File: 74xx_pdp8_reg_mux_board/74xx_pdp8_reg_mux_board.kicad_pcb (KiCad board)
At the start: 2 copper layers, 36 parts, among them P1 DIL24, P2 DIL24, P3 DIL24, P4 DIL24, P5 DIL24, P6 DIL24, U1 74LS251, U10 74LS251, U11 74LS125, U12 74LS251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

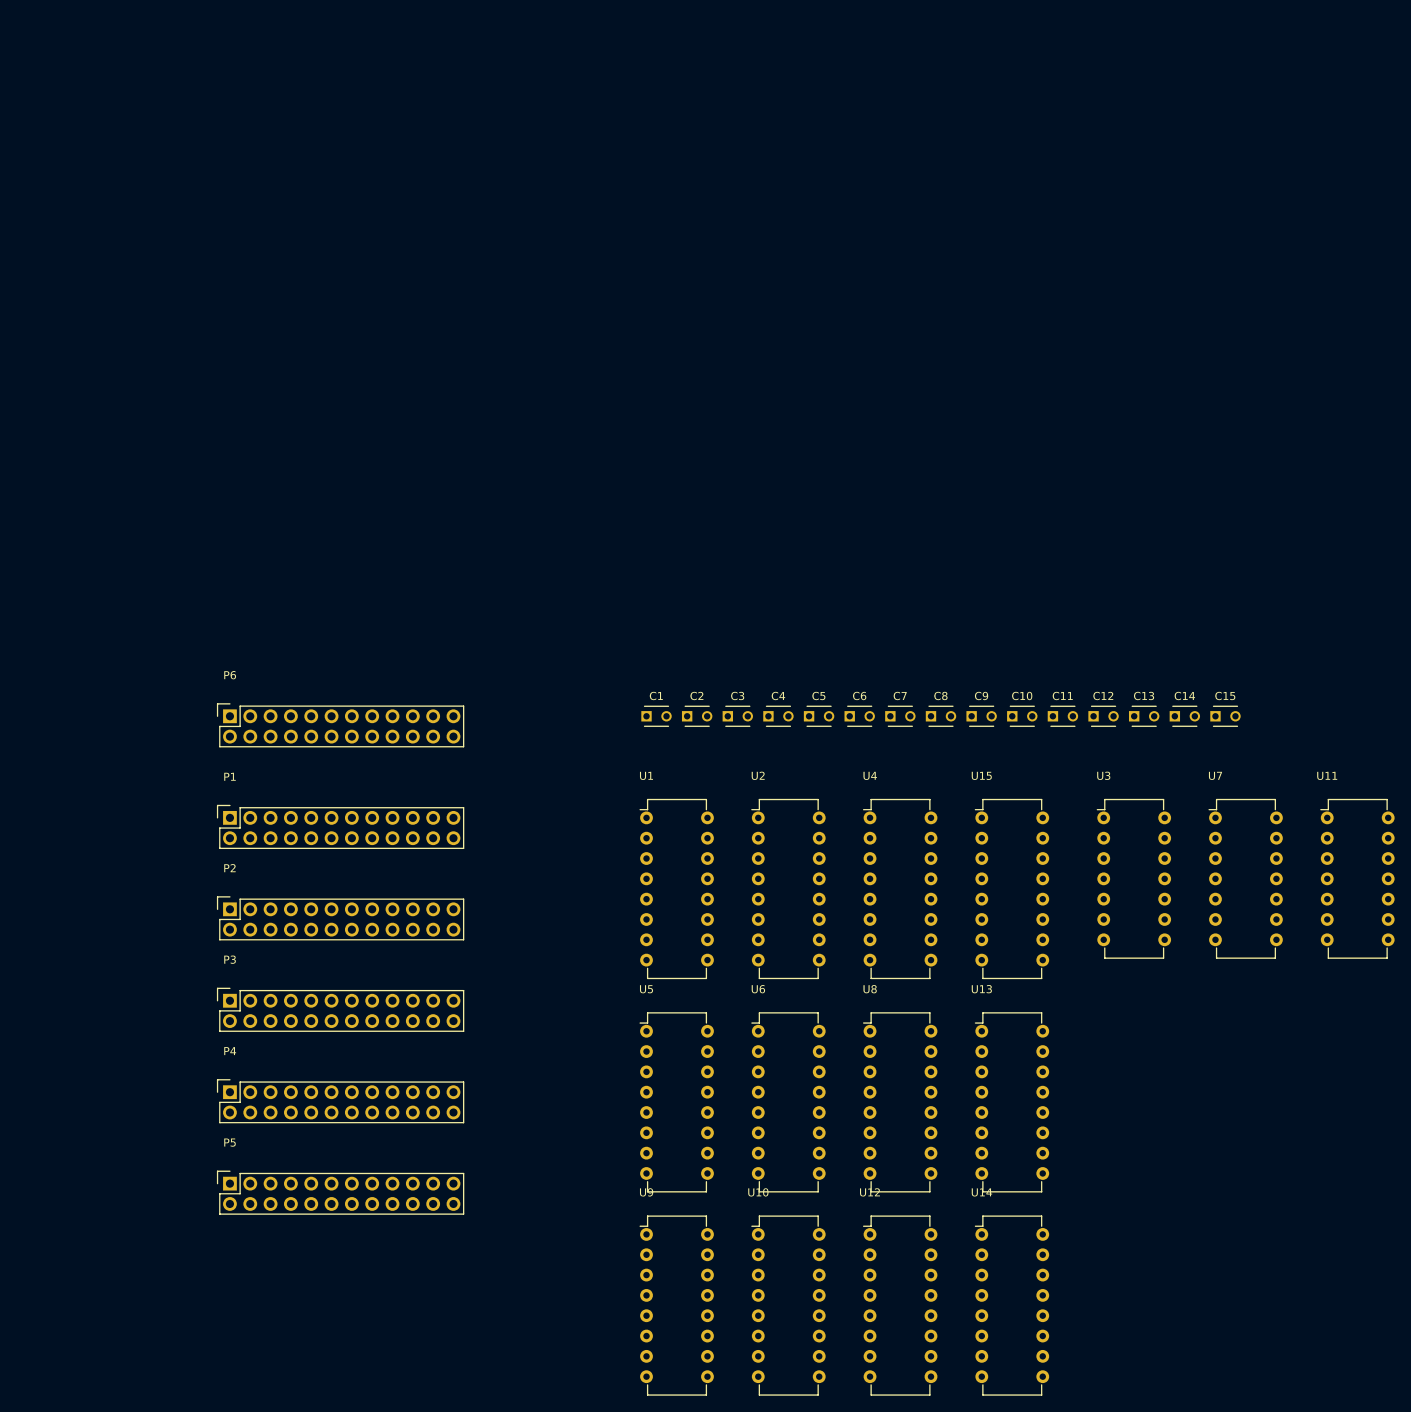
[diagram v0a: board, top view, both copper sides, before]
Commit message: Roughed-out layout of register multiplexor board. Need to double check dimensions of twin register board.
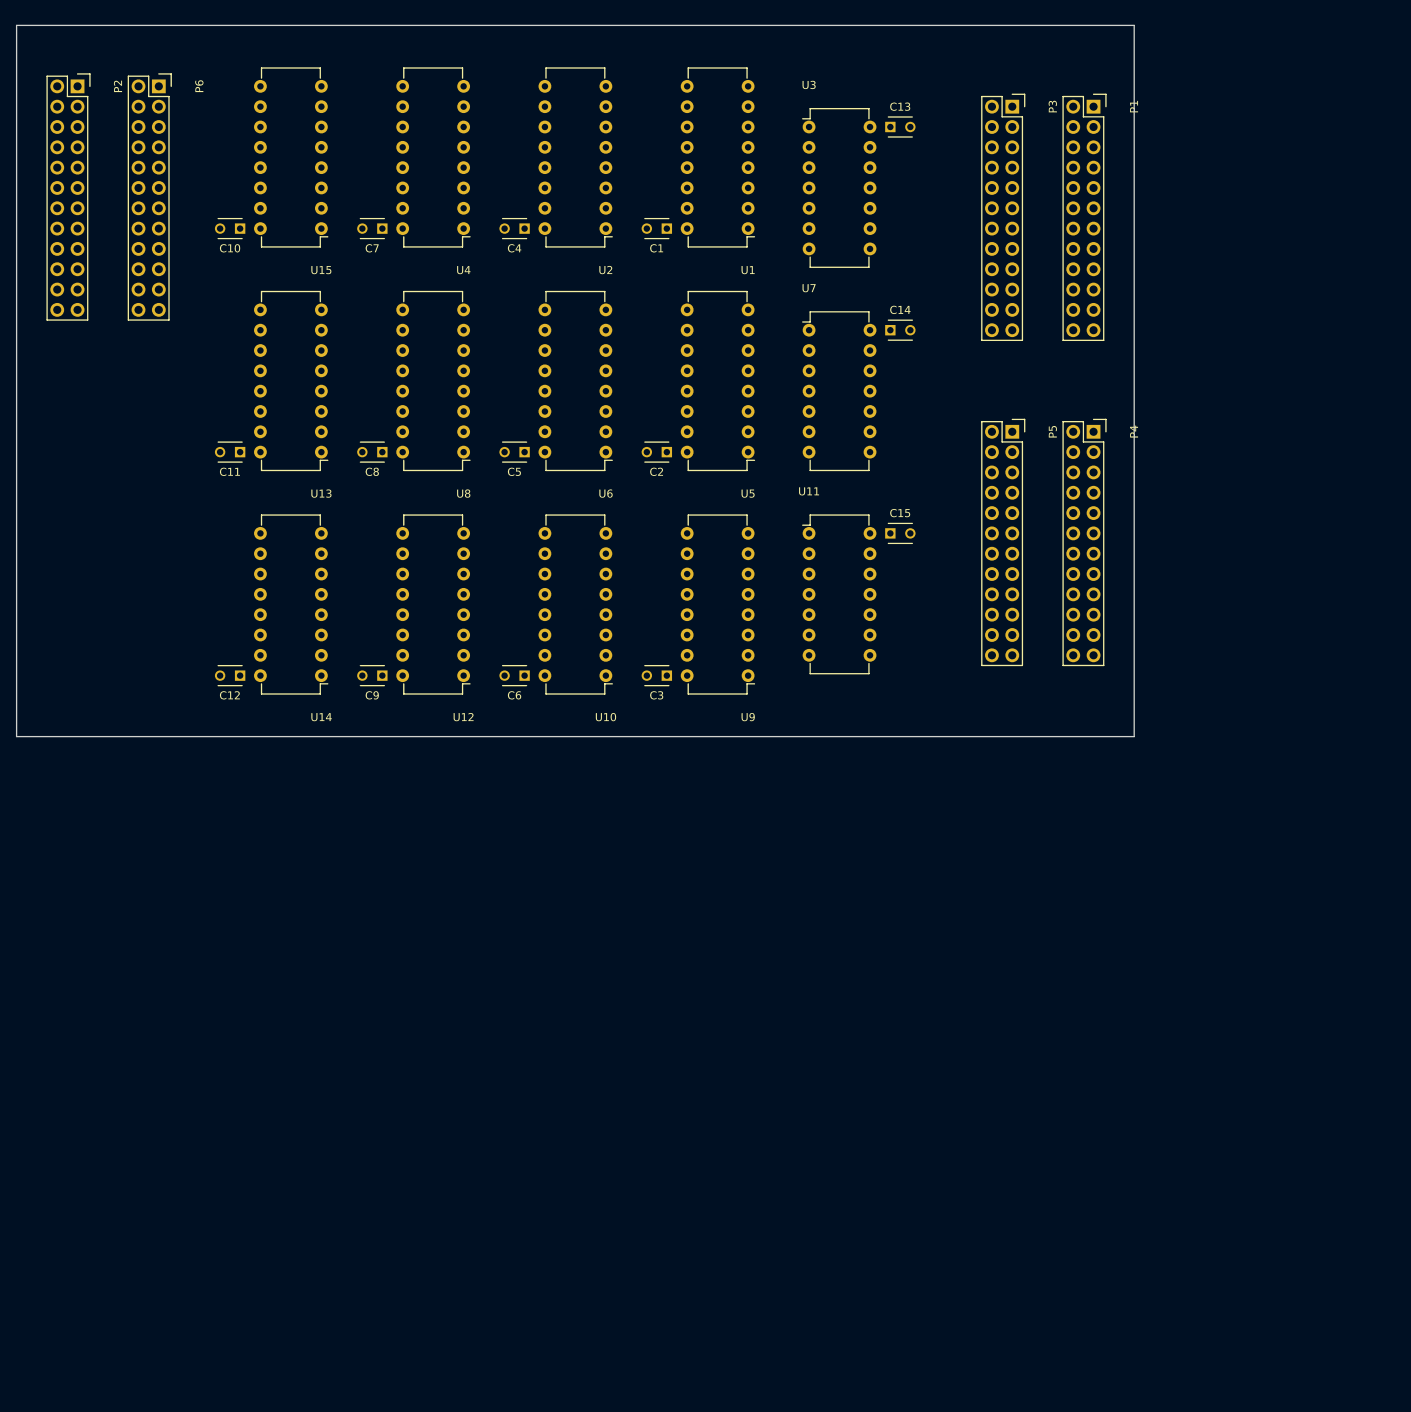
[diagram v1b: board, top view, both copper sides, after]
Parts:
- moved P3 148.5 mm to (154.9, 35.6), turned to 270 degrees
- moved P1 139.8 mm to (165.1, 35.6), turned to 270 degrees
- moved P4 135.9 mm to (165.1, 76.2), turned to 270 degrees
- moved P5 135.6 mm to (154.9, 76.2), turned to 270 degrees
- moved C10 114.2 mm to (58.4, 50.8), turned to 180 degrees
- moved U15 110.6 mm to (68.6, 50.8), turned to 180 degrees
- moved U13 109.8 mm to (68.6, 78.7), turned to 180 degrees
- moved U14 108.1 mm to (68.6, 106.7), turned to 180 degrees
- moved C11 106.8 mm to (58.4, 78.7), turned to 180 degrees
- moved C12 106.8 mm to (58.4, 106.7), turned to 180 degrees
- moved P2 104.6 mm to (38.1, 33.0), turned to 270 degrees
- moved U3 93.9 mm to (129.5, 38.1)
- moved U4 89.5 mm to (86.4, 50.8), turned to 180 degrees
- moved U8 88.4 mm to (86.4, 78.7), turned to 180 degrees
- moved C7 88.0 mm to (76.2, 50.8), turned to 180 degrees
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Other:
- board outline added: 139.7 x 88.9 mm

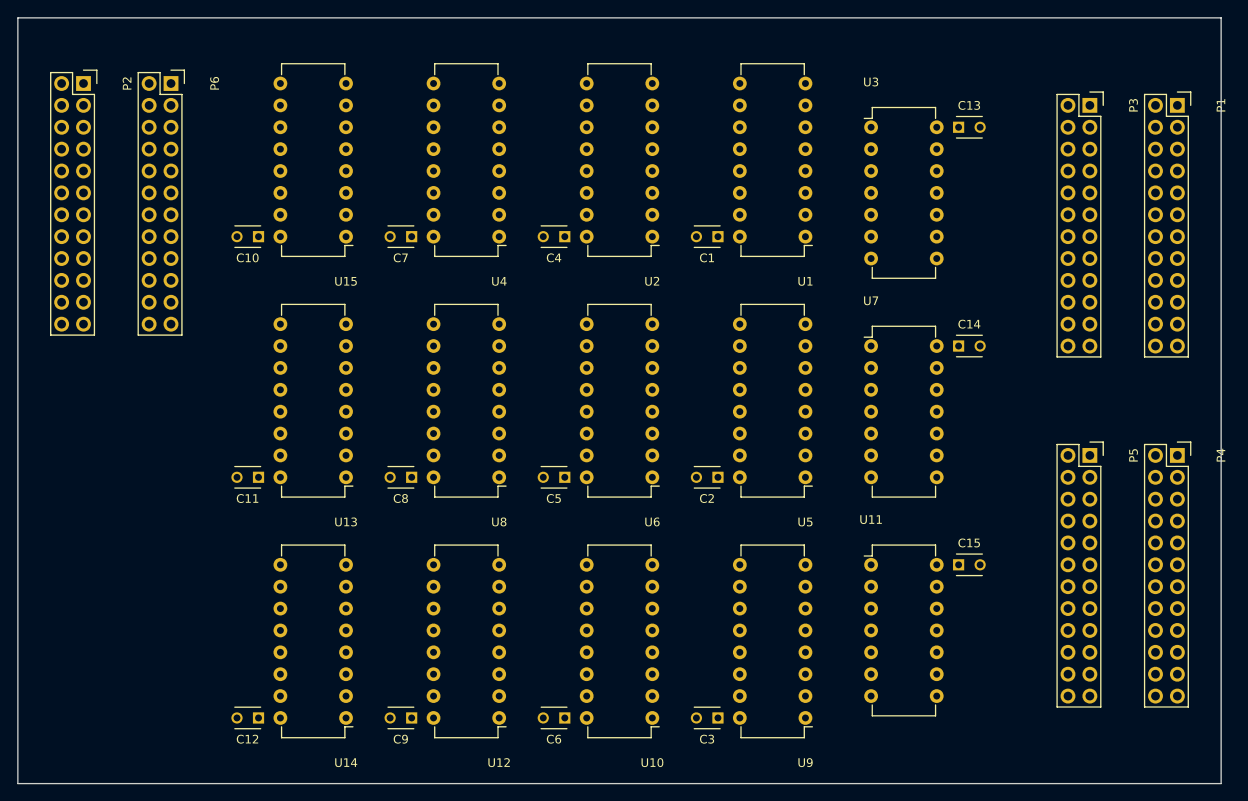
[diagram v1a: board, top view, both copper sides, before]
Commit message: Lots of tidying up. Rationalised connectors at register board 'output' end. Connectors matched on register and mux boards.
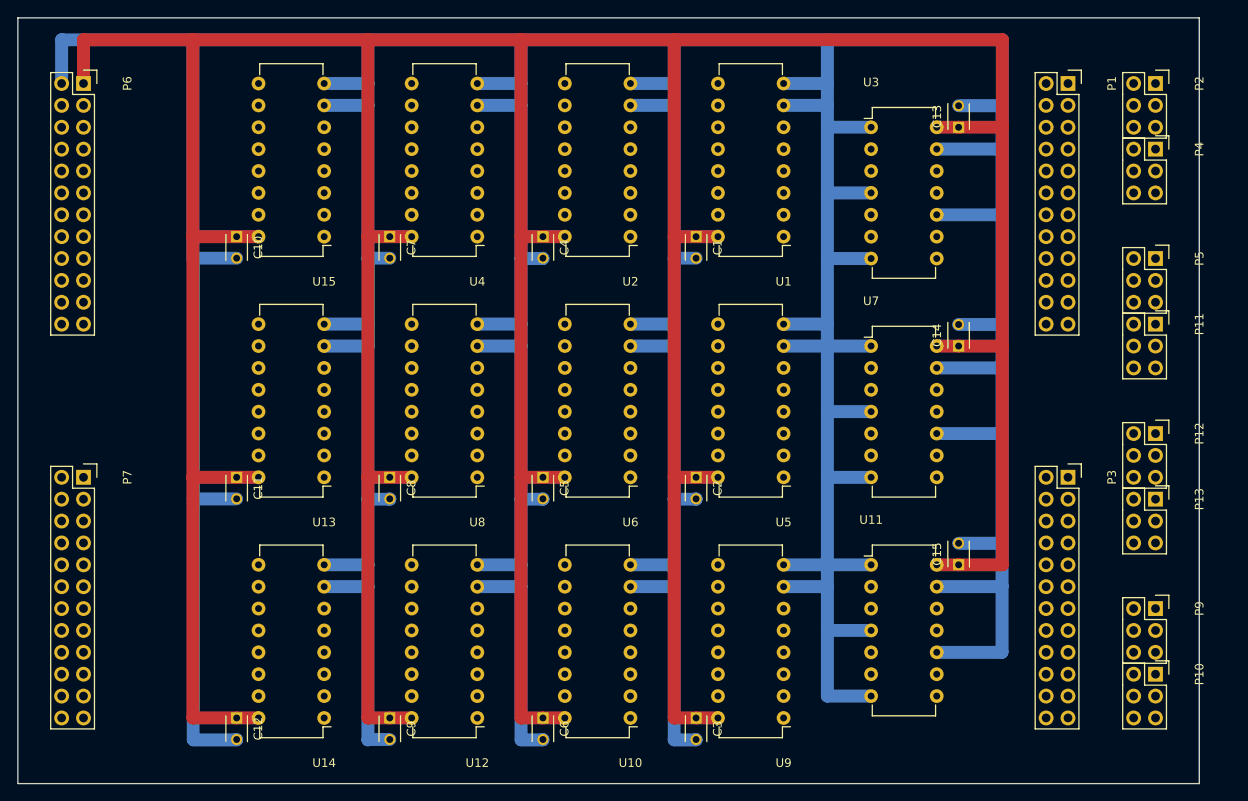
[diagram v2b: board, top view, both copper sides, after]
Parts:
- added P10: DIL6, Socket_Strips:Socket_Strip_Straight_2x03, F.Cu at (162.6, 101.6)
- added P11: DIL6, Socket_Strips:Socket_Strip_Straight_2x03, F.Cu at (162.6, 61.0)
- added P12: DIL6, Socket_Strips:Socket_Strip_Straight_2x03, F.Cu at (162.6, 73.7)
- added P13: DIL6, Socket_Strips:Socket_Strip_Straight_2x03, F.Cu at (162.6, 81.3)
- added P7: DIL24, Socket_Strips:Socket_Strip_Straight_2x12, F.Cu at (38.1, 78.7)
- added P9: DIL6, Socket_Strips:Socket_Strip_Straight_2x03, F.Cu at (162.6, 94.0)
- P2, P4, P5: value DIL24 -> DIL6; footprint Socket_Strips:Socket_Strip_Straight_2x12 -> Socket_Strips:Socket_Strip_Straight_2x03
- moved P2 124.5 mm to (162.6, 33.0)
- moved P3 43.3 mm to (152.4, 78.7)
- moved P4 35.7 mm to (162.6, 40.6)
- moved P5 24.1 mm to (162.6, 53.3)
- moved P1 13.0 mm to (152.4, 33.0)
- moved P6 10.2 mm to (38.1, 33.0)
- moved C1 2.54 mm to (109.2, 50.8), turned to 270 degrees
- moved C2 2.54 mm to (109.2, 78.7), turned to 270 degrees
- moved C3 2.54 mm to (109.2, 106.7), turned to 270 degrees
- moved C4 2.54 mm to (91.4, 50.8), turned to 270 degrees
- moved C5 2.54 mm to (91.4, 78.7), turned to 270 degrees
- moved C6 2.54 mm to (91.4, 106.7), turned to 270 degrees
- moved C7 2.54 mm to (73.7, 50.8), turned to 270 degrees
- moved C8 2.54 mm to (73.7, 78.7), turned to 270 degrees
- moved C9 2.54 mm to (73.7, 106.7), turned to 270 degrees
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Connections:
- net /IN_A_0 renamed /IN_MA_0
- net /IN_A_1 renamed /IN_MA_1
- net /IN_A_10 renamed /IN_MA_10
- net /IN_A_11 renamed /IN_MA_11
- net /IN_A_2 renamed /IN_MA_2
- net /IN_A_3 renamed /IN_MA_3
- net /IN_A_4 renamed /IN_MA_4
- net /IN_A_5 renamed /IN_MA_5
- net /IN_A_6 renamed /IN_MA_6
- net /IN_A_7 renamed /IN_MA_7
- net /IN_A_8 renamed /IN_MA_8
- net /IN_A_9 renamed /IN_MA_9
- net /IN_B_0 renamed /IN_MD_0
- net /IN_B_1 renamed /IN_MD_1
- net /IN_B_10 renamed /IN_MD_10
- net /IN_B_11 renamed /IN_MD_11
- net /IN_B_2 renamed /IN_MD_2
- net /IN_B_3 renamed /IN_MD_3
- net /IN_B_4 renamed /IN_MD_4
- net /IN_B_5 renamed /IN_MD_5
- net /IN_B_6 renamed /IN_MD_6
- net /IN_B_7 renamed /IN_MD_7
- net /IN_B_8 renamed /IN_MD_8
- net /IN_B_9 renamed /IN_MD_9
- net /IN_C_0 renamed /IN_PC_0
- net /IN_C_1 renamed /IN_PC_1
- net /IN_C_10 renamed /IN_PC_10
- net /IN_C_11 renamed /IN_PC_11
- net /IN_C_2 renamed /IN_PC_2
- net /IN_C_3 renamed /IN_PC_3
- net /IN_C_4 renamed /IN_PC_4
- net /IN_C_5 renamed /IN_PC_5
- net /IN_C_6 renamed /IN_PC_6
- net /IN_C_7 renamed /IN_PC_7
- net /IN_C_8 renamed /IN_PC_8
- net /IN_C_9 renamed /IN_PC_9
- net /IN_E_0 renamed /IN_IOT1_0
- net /IN_E_1 renamed /IN_IOT1_1
- net /IN_E_2 renamed /IN_IOT1_2
- net /IN_E_3 renamed /IN_IOT1_3
- net /IN_E_4 renamed /IN_IOT1_4
- net /IN_E_5 renamed /IN_IOT1_5
- P2 pad 1: /OUT_0 -> /IN_SR_0
- P2 pad 2: /OUT_1 -> /IN_SR_1
- P2 pad 3: /OUT_2 -> /IN_SR_2
- P2 pad 4: /OUT_3 -> /IN_SR_5
- P2 pad 5: /OUT_4 -> /IN_SR_4
- P2 pad 6: /OUT_5 -> /IN_SR_3
- P3 pad 13: /IN_D_0 -> /IN_AC_0
- P3 pad 14: /IN_D_1 -> /IN_AC_1
- P3 pad 15: /IN_D_2 -> /IN_AC_2
- P3 pad 16: /IN_D_3 -> /IN_AC_3
- P3 pad 17: /IN_D_4 -> /IN_AC_4
- P3 pad 18: /IN_D_5 -> /IN_AC_5
- P3 pad 19: /IN_D_6 -> /IN_AC_6
- P3 pad 20: /IN_D_7 -> /IN_AC_7
- P3 pad 21: /IN_D_8 -> /IN_AC_8
- P3 pad 22: /IN_D_9 -> /IN_AC_9
- P3 pad 23: /IN_D_10 -> /IN_AC_10
- P3 pad 24: /IN_D_11 -> /IN_AC_11
- P4 pad 1: /OUT_BUF_0 -> /IN_SR_6
- P4 pad 2: /OUT_BUF_1 -> /IN_SR_7
- P4 pad 3: /OUT_BUF_2 -> /IN_SR_8
- P4 pad 4: /OUT_BUF_3 -> /IN_SR_9
- P4 pad 5: /OUT_BUF_4 -> /IN_SR_10
- P4 pad 6: /OUT_BUF_5 -> /IN_SR_11
- U1 pad 1: /IN_D_0 -> /IN_SR_0
- U1 pad 14: /IN_F_0 -> /IN_IOT2_0
- U1 pad 8: (no net) -> GND
- U10 pad 1: /IN_D_7 -> /IN_SR_7
- U10 pad 14: /IN_F_7 -> /IN_IOT2_7
- U10 pad 15: /IN_E_7 -> /IN_IOT1_7
- U10 pad 8: (no net) -> GND
- U12 pad 1: /IN_D_8 -> /IN_SR_8
- U12 pad 14: /IN_F_8 -> /IN_IOT2_8
- U12 pad 15: /IN_E_8 -> /IN_IOT1_8
- U12 pad 8: (no net) -> GND
- U13 pad 1: /IN_D_9 -> /IN_SR_9
- U13 pad 14: /IN_F_9 -> /IN_IOT2_9
- U13 pad 15: /IN_E_9 -> /IN_IOT1_9
- U13 pad 8: (no net) -> GND
- U14 pad 1: /IN_D_10 -> /IN_SR_10
- U14 pad 14: /IN_F_10 -> /IN_IOT2_10
- U14 pad 15: /IN_E_10 -> /IN_IOT1_10
- U14 pad 8: (no net) -> GND
- U15 pad 1: /IN_D_11 -> /IN_SR_11
- U15 pad 14: /IN_F_11 -> /IN_IOT2_11
- U15 pad 15: /IN_E_11 -> /IN_IOT1_11
- U15 pad 8: (no net) -> GND
- U2 pad 1: /IN_D_1 -> /IN_SR_1
- U2 pad 14: /IN_F_1 -> /IN_IOT2_1
- U2 pad 8: (no net) -> GND
- U4 pad 1: /IN_D_2 -> /IN_SR_2
- U4 pad 14: /IN_F_2 -> /IN_IOT2_2
- U4 pad 8: (no net) -> GND
- U5 pad 1: /IN_D_3 -> /IN_SR_3
- U5 pad 14: /IN_F_3 -> /IN_IOT2_3
- U5 pad 8: (no net) -> GND
- U6 pad 1: /IN_D_4 -> /IN_SR_4
- U6 pad 14: /IN_F_4 -> /IN_IOT2_4
- U6 pad 8: (no net) -> GND
- U8 pad 1: /IN_D_5 -> /IN_SR_5
- U8 pad 14: /IN_F_5 -> /IN_IOT2_5
- U8 pad 8: (no net) -> GND
- U9 pad 1: /IN_D_6 -> /IN_SR_6
- U9 pad 14: /IN_F_6 -> /IN_IOT2_6
- U9 pad 15: /IN_E_6 -> /IN_IOT1_6
- U9 pad 8: (no net) -> GND
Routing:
- net GND: track 0.00 -> 853.7 mm
- net VCC: track 0.00 -> 579.1 mm
- net /S2: track 0.00 -> 33.0 mm
- net /S1: track 0.00 -> 33.0 mm
- net /S0: track 0.00 -> 33.0 mm
- net /OUT_8: track 0.00 -> 10.2 mm
- net /OUT_7: track 0.00 -> 10.2 mm
- net /OUT_6: track 0.00 -> 10.2 mm
- net /OUT_5: track 0.00 -> 10.2 mm
- net /OUT_4: track 0.00 -> 10.2 mm
- net /OUT_3: track 0.00 -> 10.2 mm
- net /OUT_1: track 0.00 -> 10.2 mm
- net /OUT_0: track 0.00 -> 10.2 mm
- net /OUT_9: track 0.00 -> 10.2 mm
- net /OUT_10: track 0.00 -> 10.2 mm
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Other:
- board size 139.7 x 88.9 mm -> 137.2 x 88.9 mm
- copper layers 2 -> 4
